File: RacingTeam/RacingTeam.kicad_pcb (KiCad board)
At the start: 4 copper layers, 122.5 x 92.5 mm, 87 parts, among them J1 BusIn, J10 BatteryIn, J11 ShutdownIn, J2 Bypass Pin, J3 BypassPin, J4 BypassPin, J5 BypassPin, J6 PC Relay, J7 AIROut, J8 Discharge Relay Out, J9 Molex, Q1 TP0610T, Q2 2N7002, Q3 2N7002, Q4 2N7002, Q4 TP0610T, Q5 2N7002, Q6 TP0610T, Q7 2N7002, Q8 TP0610T, U1 LM311, U2 LM311, U3 4N35, U4 MC78M12ABDTRKG, U6 NE555D

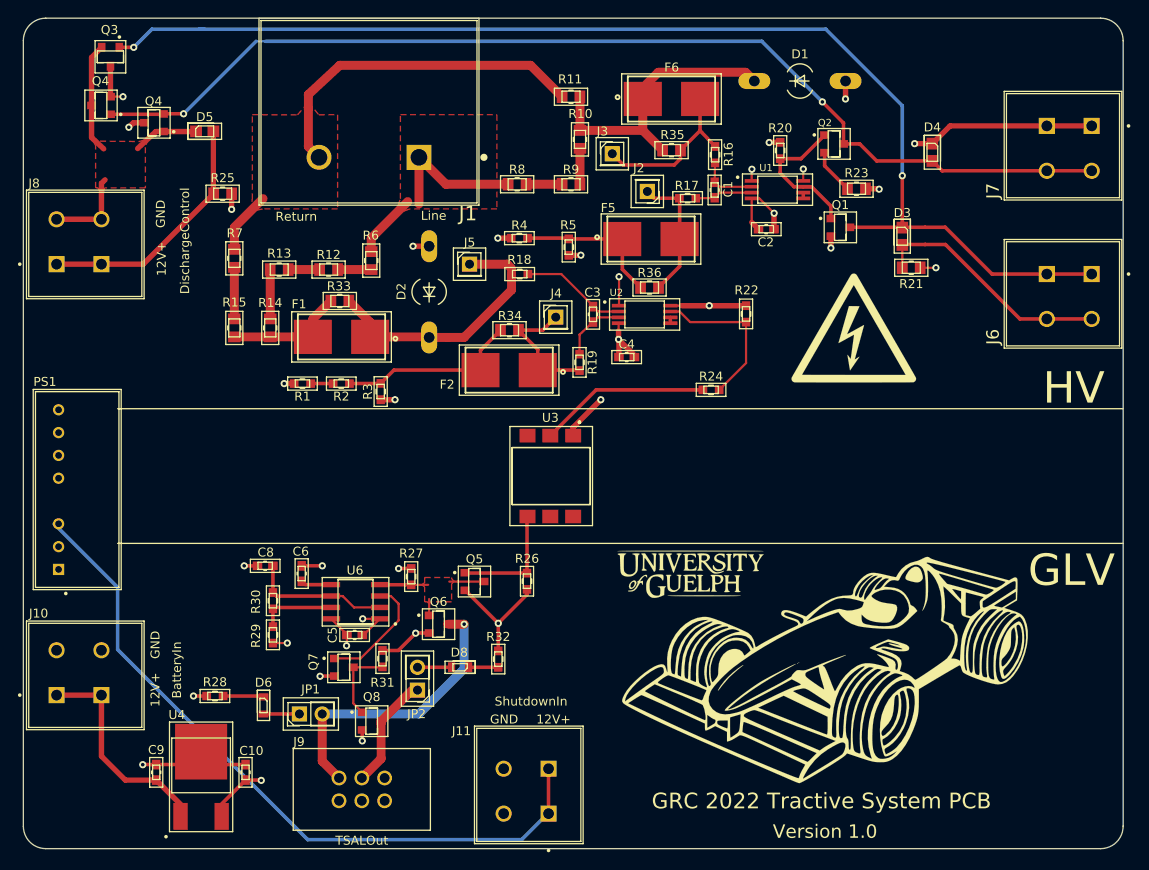
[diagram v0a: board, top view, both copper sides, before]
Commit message: Update GRC22Footprints.mod, CONV_SPBW06F-12.kicad_mod, and 43 more files...
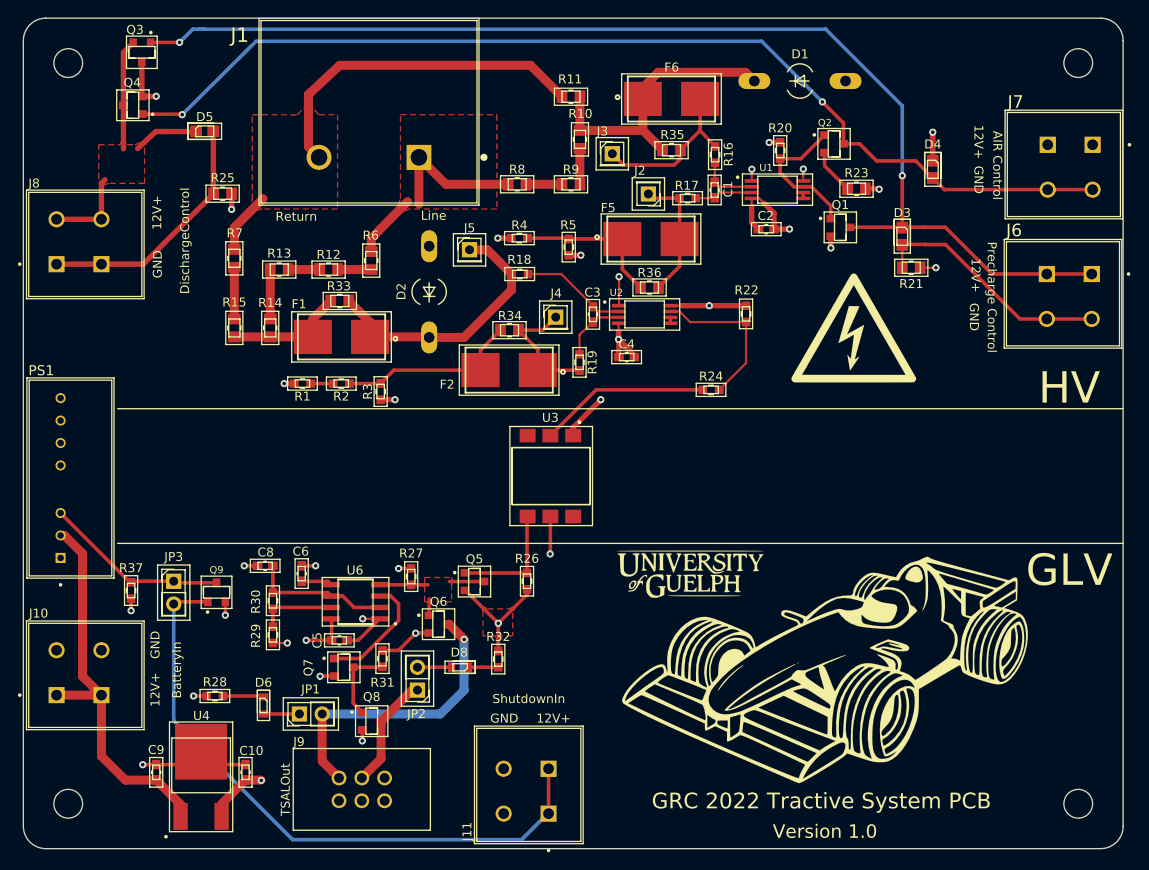
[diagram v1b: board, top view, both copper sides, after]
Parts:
- removed the Q4 at (124.0, 42.6)
- added JP3: Jumper, GRC22Footprints:PinHeader_1x02_P2.54mm_Vertical, F.Cu at (126.2, 93.7)
- added Q9: TP0610T, GRC22Footprints:2N7002H6327XTSA2_v2, F.Cu at (131.0, 95.0)
- added R37: 4kΩ, GRC22Footprints:R_0603_1608Metric_Pad0.98x0.95mm_HandSolder, F.Cu at (121.5, 94.8)
- added REF**: MountingHole_3.2mm_M3, MountingHole:MountingHole_3.2mm_M3, F.Cu at (114.5, 118.5)
- added REF**: MountingHole_3.2mm_M3, MountingHole:MountingHole_3.2mm_M3, F.Cu at (114.5, 36.0)
- added REF**: MountingHole_3.2mm_M3, MountingHole:MountingHole_3.2mm_M3, F.Cu at (227.0, 36.0)
- added REF**: MountingHole_3.2mm_M3, MountingHole:MountingHole_3.2mm_M3, F.Cu at (227.0, 118.5)
- PS1: value EC3SAW-24S12P -> SPBW06F-12; footprint GRC22Footprints:EC3SAW-24S12P -> GRC22Footprints:CONV_SPBW06F-12
- moved Q4 3.55 mm to (121.7, 40.7)
- moved Q3 3.54 mm to (122.7, 34.8)
- moved J7 2.10 mm to (228.6, 45.1)
- moved D4 1.90 mm to (210.8, 47.8)
- moved C5 1.80 mm to (144.7, 100.3)
- moved J5 1.60 mm to (159.2, 56.8)
- moved PS1 1.48 mm to (114.8, 82.2)
- moved J2 0.30 mm to (179.1, 50.6)
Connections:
- net Net-(Q5-Pad1) renamed /InvertBus
- PS1 pad 3: /Shutdown -> /Enable
- PS1 pad 5: Net-(PS1-Pad5) -> (no net)
- PS1 pad 8: Net-(PS1-Pad8) -> (no net)
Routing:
- net /Enable: track 0.00 -> 20.6 mm
- net +BATT: track 24.2 -> 44.1 mm
- net +12V: track 47.6 -> 28.9 mm, vias 10 -> 9
- net /Shutdown: track 79.9 -> 70.3 mm
- net GLV+: track 20.9 -> 28.1 mm, vias 6 -> 8
- net /PreChargeON: track 134.6 -> 130.9 mm
- net /AIRON: track 120.0 -> 117.4 mm
- net GLV-: track 39.4 -> 41.9 mm, vias 7 -> 8
- net Net-(C6-Pad1): track 3.45 -> 3.98 mm
- net GND: track 31.7 -> 31.2 mm, vias 11 -> 9
- added copper zone on F.Cu, net GLV-
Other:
- board text added: "AIR Control"
- board text added: "Precharge Control"
